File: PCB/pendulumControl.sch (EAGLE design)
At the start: 29 parts, among them IC1 PIC32MX340F512H, IC2 LT1963EST-3.3

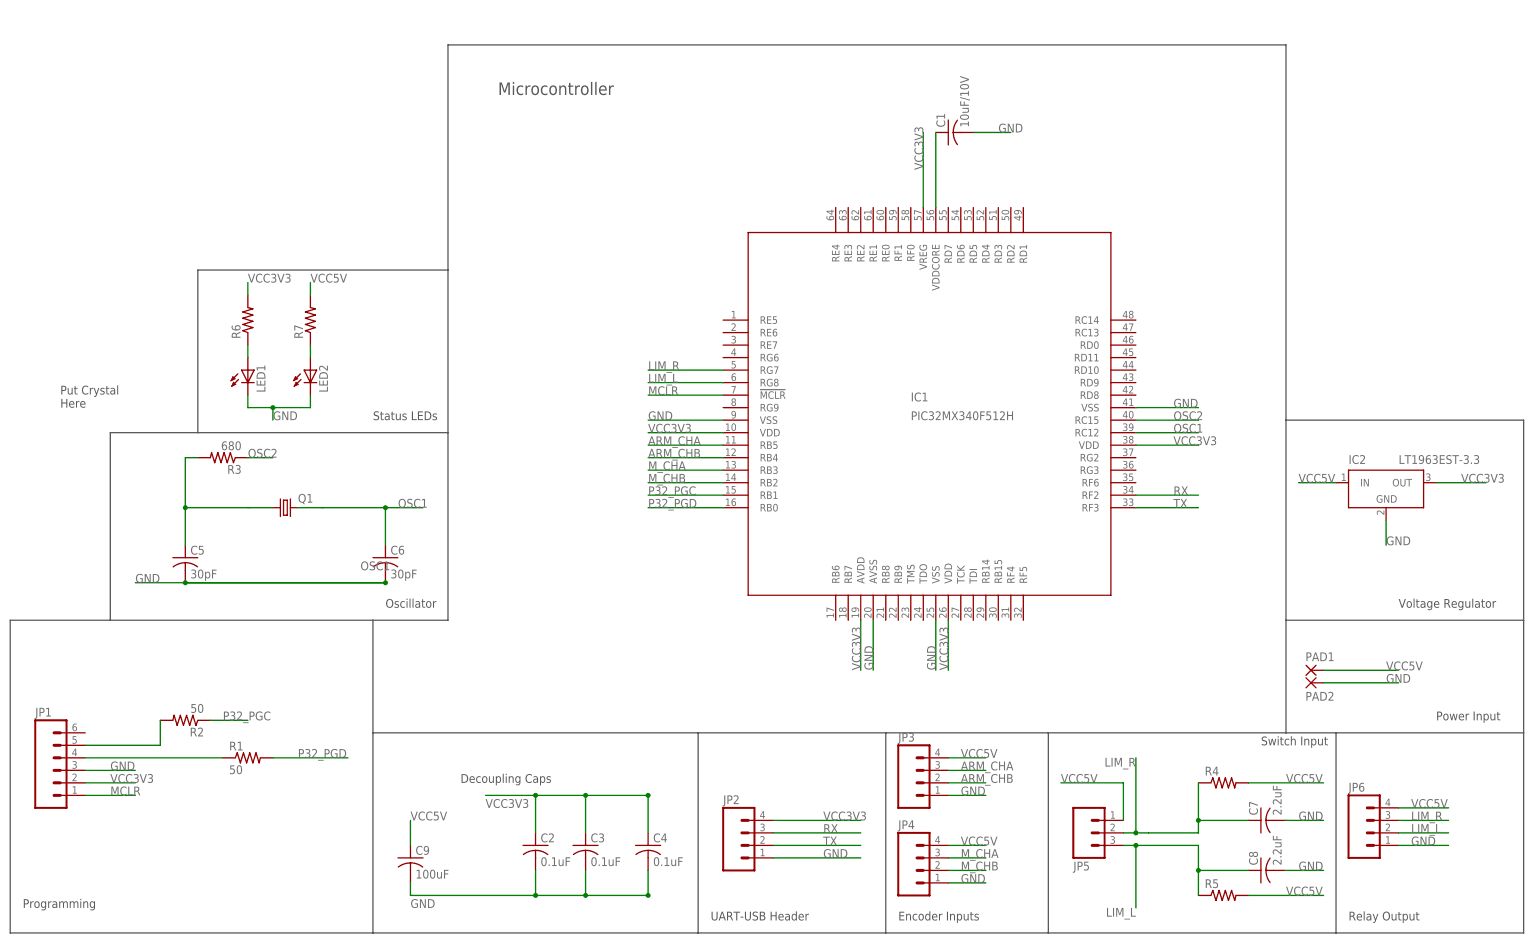
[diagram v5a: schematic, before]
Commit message: Added MCLR circuit and moved silk screen text around
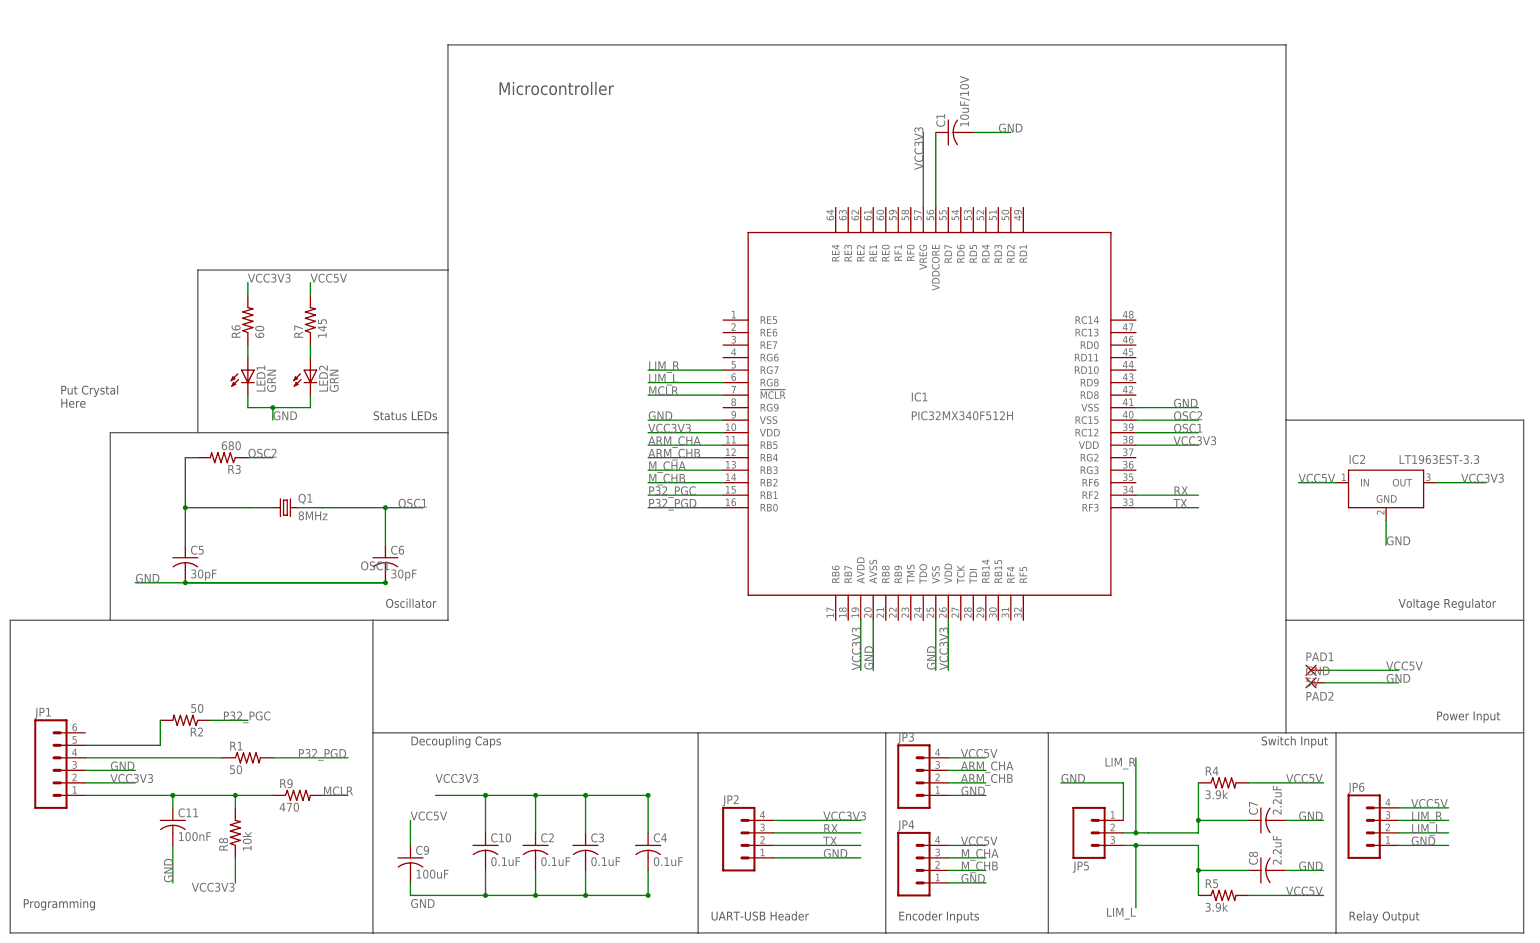
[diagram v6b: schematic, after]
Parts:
- added C10: 0.1uF, rcl:C-USC0805
- added C11: 100nF, rcl:C-USC0805
- added R8: 10k, resistor:R-US_R0805
- added R9: 470, resistor:R-US_R0805
- LED1, LED2: value (none) -> GRN
- PAD1: value (none) -> 5V
- PAD2: value (none) -> GND
- Q1: value (none) -> 8MHz
- R4, R5: value (none) -> 3.9k
- R6: value (none) -> 60
- R7: value (none) -> 145
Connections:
- new net N$6: C11.1, JP1.1, R8.2, R9.1
- net GND: now also C10.2, C11.2, JP5.1
- net MCLR: now also R9.2; no longer JP1.1
- net VCC3V3: now also C10.1, R8.1
- net VCC5V: no longer JP5.1
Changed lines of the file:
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@@
 <?xml version="1.0" encoding="utf-8"?>
 <!DOCTYPE eagle SYSTEM "eagle.dtd">
-<eagle version="7.2.0">
+<eagle version="7.3.0">
 <drawing>
 <settings>
@@
 <part name="JP4" library="SparkFun-Connectors" deviceset="M04" device="PTH"/>
 <part name="JP5" library="SparkFun-Connectors" deviceset="M03" device="PTH"/>
-<part name="R4" library="rcl" deviceset="R-US_" device="R0805"/>
-<part name="R5" library="rcl" deviceset="R-US_" device="R0805"/>
+<part name="R4" library="rcl" deviceset="R-US_" device="R0805" value="3.9k"/>
+<part name="R5" library="rcl" deviceset="R-US_" device="R0805" value="3.9k"/>
 <part name="C7" library="rcl" deviceset="C-US" device="C0805" value="2.2uF"/>
 <part name="C8" library="rcl" deviceset="C-US" device="C0805" value="2.2uF"/>
 <part name="JP6" library="SparkFun-Connectors" deviceset="M04" device="PTH"/>
 <part name="C9" library="rcl" deviceset="C-US" device="C0805" value="100uF"/>
-<part name="LED1" library="led" deviceset="LED" device="CHIP-LED0805"/>
-<part name="LED2" library="led" deviceset="LED" device="CHIP-LED0805"/>
-<part name="R6" library="rcl" deviceset="R-US_" device="R0805"/>
-<part name="R7" library="rcl" deviceset="R-US_" device="R0805"/>
+<part name="LED1" library="led" deviceset="LED" device="CHIP-LED0805" value="GRN"/>
+<part name="LED2" library="led" deviceset="LED" device="CHIP-LED0805" value="GRN"/>
+<part name="R6" library="rcl" deviceset="R-US_" device="R0805" value="60"/>
+<part name="R7" library="rcl" deviceset="R-US_" device="R0805" value="145"/>
 <part name="IC2" library="linear-technology" deviceset="LT1963EST" device="" technology="-3.3"/>
-<part name="Q1" library="crystal" deviceset="CRYSTAL" device="HC49S"/>
-<part name="PAD1" library="wirepad" deviceset="3,81/1,4" device=""/>
-<part name="PAD2" library="wirepad" deviceset="3,81/1,4" device=""/>
+<part name="Q1" library="crystal" deviceset="CRYSTAL" device="HC49S" value="8MHz"/>
+<part name="PAD1" library="wirepad" deviceset="3,81/1,4" device="" value="5V"/>
+<part name="PAD2" library="wirepad" deviceset="3,81/1,4" device="" value="GND"/>
+<part name="C10" library="rcl" deviceset="C-US" device="C0805" value="0.1uF"/>
+<part name="C11" library="rcl" deviceset="C-US" device="C0805" value="100nF"/>
+<part name="R8" library="resistor" deviceset="R-US_" device="R0805" value="10k"/>
+<part name="R9" library="resistor" deviceset="R-US_" device="R0805" value="470"/>
 </parts>
 <sheets>
@@
 <wire x1="-38.1" y1="-27.94" x2="27.94" y2="-27.94" width="0.1524" layer="97"/>
 <wire x1="27.94" y1="-27.94" x2="27.94" y2="-68.58" width="0.1524" layer="97"/>
-<text x="-20.32" y="-38.1" size="1.778" layer="97">Decoupling Caps</text>
+<text x="-30.48" y="-30.48" size="1.778" layer="97">Decoupling Caps</text>
 <wire x1="-91.44" y1="-5.08" x2="-91.44" y2="33.02" width="0.1524" layer="97"/>
 <wire x1="-73.66" y1="33.02" x2="-22.86" y2="33.02" width="0.1524" layer="97"/>
@@
 <instance part="PAD1" gate="1" x="152.4" y="-15.24"/>
 <instance part="PAD2" gate="1" x="152.4" y="-17.78" rot="MR180"/>
+<instance part="C10" gate="G$1" x="-15.24" y="-50.8"/>
+<instance part="C11" gate="G$1" x="-78.74" y="-45.72"/>
+<instance part="R8" gate="G$1" x="-66.04" y="-48.26" rot="R90"/>
+<instance part="R9" gate="G$1" x="-53.34" y="-40.64"/>
 </instances>
 <busses>
@@
 </segment>
 <segment>
-<pinref part="JP1" gate="G$1" pin="1"/>
-<wire x1="-96.52" y1="-40.64" x2="-86.36" y2="-40.64" width="0.1524" layer="91"/>
-<label x="-91.44" y="-40.64" size="1.778" layer="95"/>
+<pinref part="R9" gate="G$1" pin="2"/>
+<wire x1="-48.26" y1="-40.64" x2="-43.18" y2="-40.64" width="0.1524" layer="91"/>
+<label x="-48.26" y="-40.64" size="1.778" layer="95"/>
 </segment>
 </net>
@@
 <label x="-30.48" y="-63.5" size="1.778" layer="95"/>
 <pinref part="C9" gate="G$1" pin="2"/>
-<wire x1="-5.08" y1="-60.96" x2="-30.48" y2="-60.96" width="0.1524" layer="91"/>
+<wire x1="-5.08" y1="-60.96" x2="-15.24" y2="-60.96" width="0.1524" layer="91"/>
+<wire x1="-15.24" y1="-60.96" x2="-30.48" y2="-60.96" width="0.1524" layer="91"/>
 <wire x1="-30.48" y1="-60.96" x2="-30.48" y2="-58.42" width="0.1524" layer="91"/>
+<junction x="-15.24" y="-60.96"/>
+<pinref part="C10" gate="G$1" pin="2"/>
+<wire x1="-15.24" y1="-60.96" x2="-15.24" y2="-55.88" width="0.1524" layer="91"/>
 </segment>
 <segment>
@@
 <wire x1="167.64" y1="15.24" x2="167.64" y2="10.16" width="0.1524" layer="91"/>
 <label x="167.64" y="10.16" size="1.778" layer="95"/>
+</segment>
+<segment>
+<pinref part="JP5" gate="G$1" pin="1"/>
+<wire x1="114.3" y1="-45.72" x2="114.3" y2="-38.1" width="0.1524" layer="91"/>
+<wire x1="114.3" y1="-38.1" x2="101.6" y2="-38.1" width="0.1524" layer="91"/>
+<label x="101.6" y="-38.1" size="1.778" layer="95"/>
+</segment>
+<segment>
+<pinref part="C11" gate="G$1" pin="2"/>
+<wire x1="-78.74" y1="-50.8" x2="-78.74" y2="-58.42" width="0.1524" layer="91"/>
+<label x="-78.74" y="-58.42" size="1.778" layer="95" rot="R90"/>
 </segment>
 </net>
@@
 <junction x="5.08" y="-40.64"/>
 <junction x="17.78" y="-40.64"/>
-<label x="-15.24" y="-43.18" size="1.778" layer="95"/>
+<label x="-25.4" y="-38.1" size="1.778" layer="95"/>
+<pinref part="C10" gate="G$1" pin="1"/>
+<wire x1="-15.24" y1="-48.26" x2="-15.24" y2="-40.64" width="0.1524" layer="91"/>
+<wire x1="-15.24" y1="-40.64" x2="-25.4" y2="-40.64" width="0.1524" layer="91"/>
+<junction x="-15.24" y="-40.64"/>
 </segment>
 <segment>
@@
 <wire x1="60.96" y1="-5.08" x2="60.96" y2="-15.24" width="0.1524" layer="91"/>
 <label x="60.96" y="-15.24" size="1.778" layer="95" rot="R90"/>
+</segment>
+<segment>
+<pinref part="R8" gate="G$1" pin="1"/>
+<wire x1="-66.04" y1="-53.34" x2="-66.04" y2="-58.42" width="0.1524" layer="91"/>
+<label x="-66.04" y="-58.42" size="1.778" layer="95" rot="R180"/>
 </segment>
 </net>
@@
 <label x="149.86" y="22.86" size="1.778" layer="95"/>
 </segment>
-<segment>
-<pinref part="JP5" gate="G$1" pin="1"/>
-<wire x1="114.3" y1="-45.72" x2="114.3" y2="-38.1" width="0.1524" layer="91"/>
-<wire x1="114.3" y1="-38.1" x2="101.6" y2="-38.1" width="0.1524" layer="91"/>
-<label x="101.6" y="-38.1" size="1.778" layer="95"/>
-</segment>
 </net>
 <net name="N$4" class="0">
@@
 </segment>
 </net>
+<net name="N$6" class="0">
+<segment>
+<pinref part="R9" gate="G$1" pin="1"/>
+<pinref part="R8" gate="G$1" pin="2"/>
+<wire x1="-78.74" y1="-40.64" x2="-66.04" y2="-40.64" width="0.1524" layer="91"/>
+<wire x1="-66.04" y1="-40.64" x2="-58.42" y2="-40.64" width="0.1524" layer="91"/>
+<wire x1="-66.04" y1="-43.18" x2="-66.04" y2="-40.64" width="0.1524" layer="91"/>
+<pinref part="C11" gate="G$1" pin="1"/>
+<wire x1="-78.74" y1="-43.18" x2="-78.74" y2="-40.64" width="0.1524" layer="91"/>
+<junction x="-66.04" y="-40.64"/>
+<pinref part="JP1" gate="G$1" pin="1"/>
+<wire x1="-96.52" y1="-40.64" x2="-78.74" y2="-40.64" width="0.1524" layer="91"/>
+<junction x="-78.74" y="-40.64"/>
+</segment>
+</net>
 </nets>
 </sheet>
 </sheets>
+<errors>
+</errors>
 </schematic>
 </drawing>

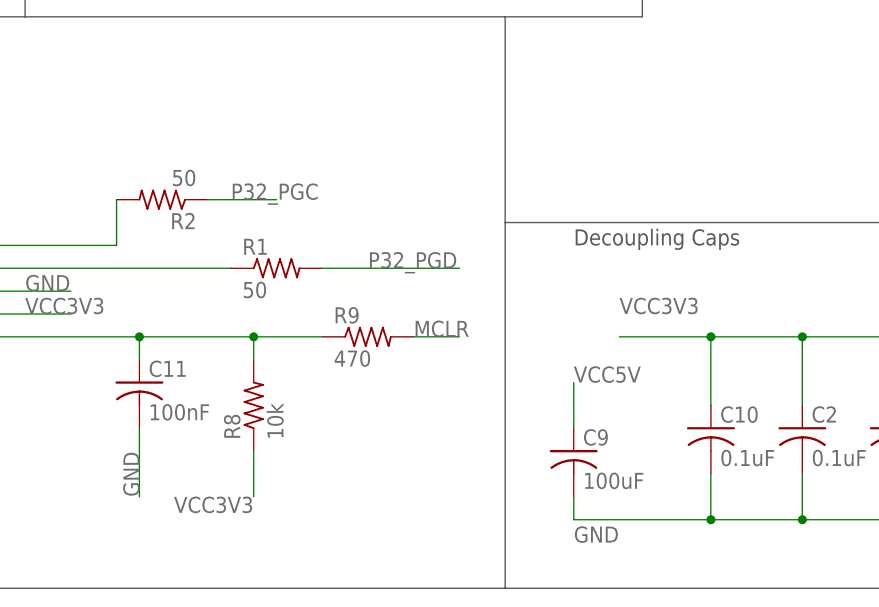
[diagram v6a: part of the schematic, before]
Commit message: Finished BOM and moved oscillator closer to the microcontroller
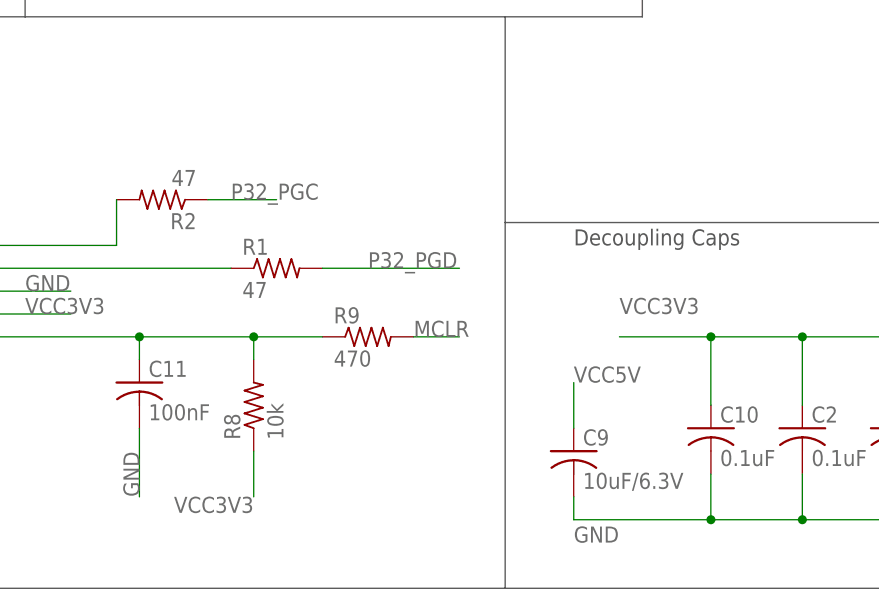
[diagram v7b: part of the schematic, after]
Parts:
- C9: value 100uF -> 10uF/6.3V
- R1, R2: value 50 -> 47
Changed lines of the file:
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@@
 <part name="C1" library="rcl" deviceset="C-US" device="C0805" value="10uF/10V"/>
 <part name="JP1" library="SparkFun-Connectors" deviceset="M06" device="FEMALE_LOCK"/>
-<part name="R1" library="resistor" deviceset="R-US_" device="R0805" value="50"/>
-<part name="R2" library="resistor" deviceset="R-US_" device="R0805" value="50"/>
+<part name="R1" library="resistor" deviceset="R-US_" device="R0805" value="47"/>
+<part name="R2" library="resistor" deviceset="R-US_" device="R0805" value="47"/>
 <part name="C2" library="resistor" deviceset="C-US" device="C0805" value="0.1uF"/>
 <part name="C3" library="resistor" deviceset="C-US" device="C0805" value="0.1uF"/>
@@
 <part name="C8" library="rcl" deviceset="C-US" device="C0805" value="2.2uF"/>
 <part name="JP6" library="SparkFun-Connectors" deviceset="M04" device="PTH"/>
-<part name="C9" library="rcl" deviceset="C-US" device="C0805" value="100uF"/>
+<part name="C9" library="rcl" deviceset="C-US" device="C0805" value="10uF/6.3V"/>
 <part name="LED1" library="led" deviceset="LED" device="CHIP-LED0805" value="GRN"/>
 <part name="LED2" library="led" deviceset="LED" device="CHIP-LED0805" value="GRN"/>
